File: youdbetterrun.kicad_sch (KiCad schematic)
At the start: 0 parts

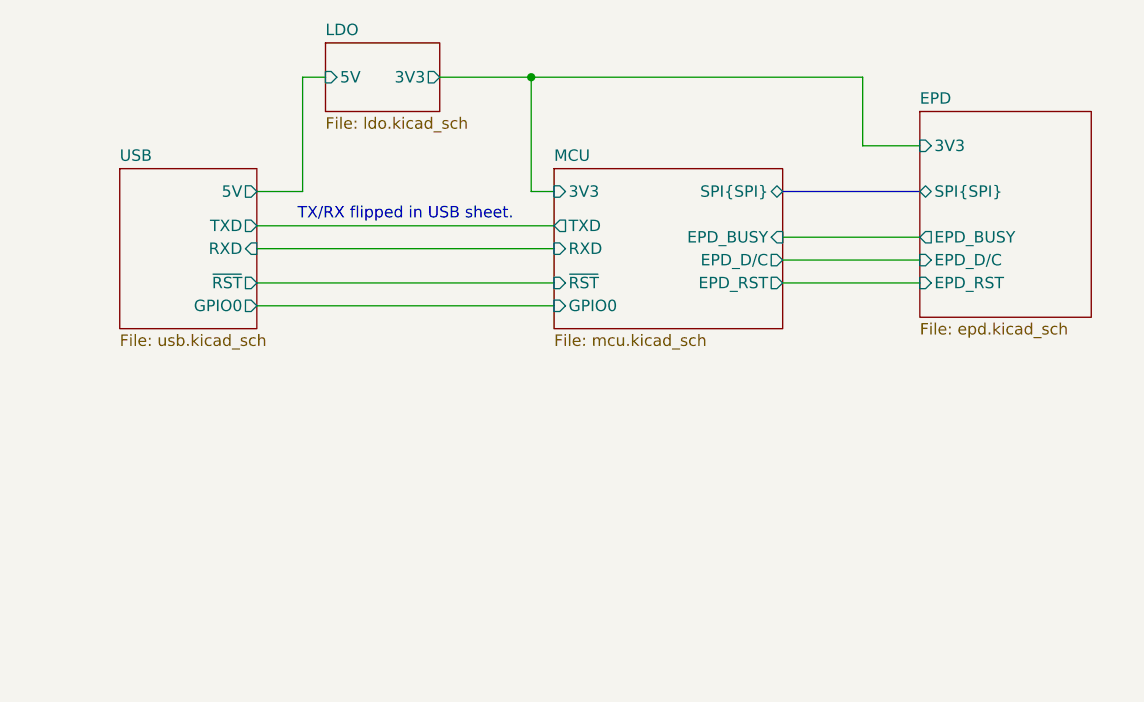
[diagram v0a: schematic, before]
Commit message: Switch to ESP32
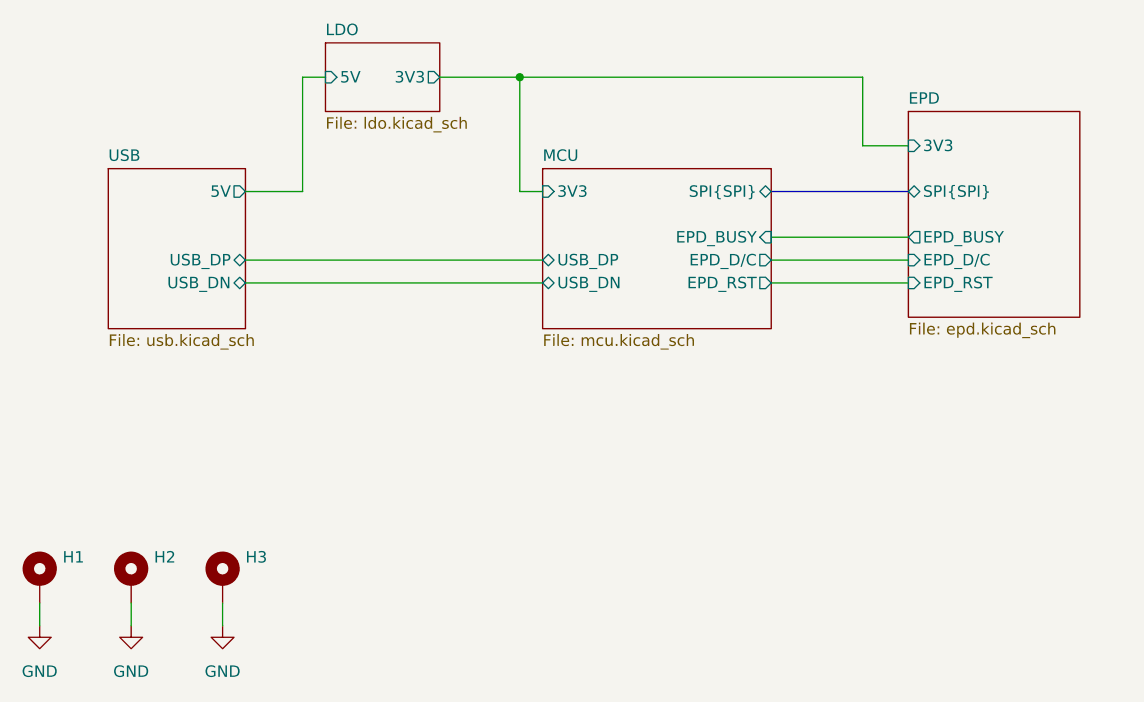
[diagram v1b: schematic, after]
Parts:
- added H1, H2, H3: MountingHole_Pad, MountingHole:MountingHole_2.2mm_M2_Pad, symbol Mechanical:MountingHole_Pad
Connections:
- new net GND: H1.1, H2.1, H3.1
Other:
- sheet MCU ports: added USB_DN, USB_DP; removed GPIO0, RXD, TXD, ~{RST}
- sheet USB ports: added USB_DN, USB_DP; removed GPIO0, RXD, TXD, ~{RST}
- note removed: "TX/RX flipped in USB sheet."
- company: (none) -> Marcel Robitaille
- title: (none) -> Top Level

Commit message: WIP
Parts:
- added H4: MountingHole_Pad, MountingHole:MountingHole_2.2mm_M2_Pad, symbol Mechanical:MountingHole_Pad
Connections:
- net GND: now also H4.1
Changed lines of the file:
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@@
+	(wire
+		(pts
+			(xy 66.04 101.6) (xy 66.04 104.14)
+		)
+		(stroke
+			(width 0)
+			(type default)
+		)
+	)
 	(wire
 		(pts
@@
 			(width 0)
 			(type default)
+		)
+	)
+	(symbol
+		(lib_id "power:GND")
+		(at 66.04 104.14 0)
+		(unit 1)
+		(exclude_from_sim no)
+		(in_bom yes)
+		(on_board yes)
+		(dnp no)
+		(fields_autoplaced yes)
+		(property "Reference" "#PWR035"
+			(at 66.04 110.49 0)
+			(effects
+				(font
+					(size 1.27 1.27)
+				)
+				(hide yes)
+			)
+		)
+		(property "Value" "GND"
+			(at 66.04 109.22 0)
+			(effects
+				(font
+					(size 1.27 1.27)
+				)
+			)
+		)
+		(property "Footprint" ""
+			(at 66.04 104.14 0)
+			(effects
+				(font
+					(size 1.27 1.27)
+				)
+				(hide yes)
+			)
+		)
+		(property "Datasheet" ""
+			(at 66.04 104.14 0)
+			(effects
+				(font
+					(size 1.27 1.27)
+				)
+				(hide yes)
+			)
+		)
+		(property "Description" "Power symbol creates a global label with name \"GND\" , ground"
+			(at 66.04 104.14 0)
+			(effects
+				(font
+					(size 1.27 1.27)
+				)
+				(hide yes)
+			)
+		)
+		(pin "1"
+		)
+		(instances
+			(project "youdbetterrun"
+				(path "/50da2b4e-34b1-4787-8ee6-5d7d17f804f4"
+					(reference "#PWR035")
+					(unit 1)
+				)
+			)
 		)
 	)
@@
 					(unit 1)
 				)
+			)
+		)
+	)
+	(symbol
+		(lib_id "Mechanical:MountingHole_Pad")
+		(at 66.04 99.06 0)
+		(unit 1)
+		(exclude_from_sim no)
+		(in_bom no)
+		(on_board yes)
+		(dnp no)
+		(fields_autoplaced yes)
+		(property "Reference" "H4"
+			(at 68.58 96.5199 0)
+			(effects
+				(font
+					(size 1.27 1.27)
+				)
+				(justify left)
+			)
+		)
+		(property "Value" "MountingHole_Pad"
+			(at 68.58 99.0599 0)
+			(effects
+				(font
+					(size 1.27 1.27)
+				)
+				(justify left)
+				(hide yes)
+			)
+		)
+		(property "Footprint" "MountingHole:MountingHole_2.2mm_M2_Pad"
+			(at 66.04 99.06 0)
+			(effects
+				(font
+					(size 1.27 1.27)
+				)
+				(hide yes)
+			)
+		)
+		(property "Datasheet" "~"
+			(at 66.04 99.06 0)
+			(effects
+				(font
+					(size 1.27 1.27)
+				)
+				(hide yes)
+			)
+		)
+		(property "Description" "Mounting Hole with connection"
+			(at 66.04 99.06 0)
+			(effects
+				(font
+					(size 1.27 1.27)
+				)
+				(hide yes)
+			)
+		)
+		(pin "1"
+		)
+		(instances
+			(project "youdbetterrun"
+				(path "/50da2b4e-34b1-4787-8ee6-5d7d17f804f4"
+					(reference "H4")
+					(unit 1)
+				)
